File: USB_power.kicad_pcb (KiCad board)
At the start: 2 copper layers, 13 parts, among them J1 PWR_IN, J2 USB_A

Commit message: 配線完了
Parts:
- removed C3, C4: 1uF, Capacitor_SMD:C_0805_2012Metric
- added C10: 10uF, Capacitor_SMD:C_0805_2012Metric, F.Cu at (61.2, 73.7)
- added J4: USB_C_Receptacle_USB2.0_16P, Connector_USB:USB_C_Receptacle_GCT_USB4105-xx-A_16P_TopMnt_Horizontal, F.Cu at (79.0, 99.1)
- added MD2: OKL-T_6-W12N-C, USB_power:MURATA_OKL-T-6-W12N-C_0, F.Cu at (53.3, 80.0)
- added R10: 200R, Resistor_SMD:R_0805_2012Metric, F.Cu at (63.3, 79.3)
- added R6: 1k, Resistor_SMD:R_0805_2012Metric, F.Cu at (61.5, 86.3)
- added R7: 330R, Resistor_SMD:R_0805_2012Metric, F.Cu at (63.5, 84.4)
- added R8: 10R, Resistor_SMD:R_0805_2012Metric, F.Cu at (65.5, 82.7)
- added R9: 1k, Resistor_SMD:R_0805_2012Metric, F.Cu at (61.3, 77.5)
- C1, C2: value 10uF -> 22uF
- J2: value USB_A -> USB_A_Stacked; footprint Connector_USB:USB_A_CONNFLY_DS1095-WNR0 -> Connector_USB:USB_A_CUI_UJ2-ADH-TH_Horizontal_Stacked
- MD1: footprint Pi_Header:MURATA_OKL-T-6-W12N-C_0 -> USB_power:MURATA_OKL-T-6-W12N-C_0
- moved C1 34.3 mm to (52.3, 91.4)
- moved R5 33.3 mm to (63.5, 99.0), turned to -90 degrees
- moved R4 30.9 mm to (61.4, 97.0), turned to -90 degrees
- moved MD1 30.9 mm to (53.6, 99.6)
- moved R1 30.9 mm to (61.7, 105.8)
- moved R2 30.8 mm to (63.8, 104.0)
- moved R3 30.7 mm to (65.8, 102.2)
- moved C5 28.7 mm to (61.5, 93.5), turned to -90 degrees
- moved C2 22.1 mm to (52.3, 71.9)
- moved J1 18.7 mm to (51.0, 62.2), turned to 0 degrees
- moved J2 16.9 mm to (69.8, 75.4), turned to 180 degrees
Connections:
- J2 pad 1: +5V -> +5VP
- J2 pad 5: GND -> +5VP
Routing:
- net GND: track 0.00 -> 60.3 mm, vias 30 -> 11
- net +5V: track 0.00 -> 33.7 mm, vias 4 -> 0
- net +5VP: track 0.00 -> 12.5 mm
- net Net-(MD2-TRIM): track 0.00 -> 4.63 mm
- net Net-(R4-Pad2): track 0.00 -> 2.12 mm
- net Net-(R7-Pad2): track 0.00 -> 2.05 mm
- net Net-(R10-Pad1): track 0.00 -> 2.03 mm
- net Net-(R6-Pad2): track 0.00 -> 2.03 mm
- net Net-(MD1-TRIM): track 5.52 -> 4.63 mm
- added copper zone on B.Cu, net +5VP
- added copper zone on F.Cu, net +5VP
- removed copper zone on B.Cu, net +5V
- removed copper zone on F.Cu, net +5V

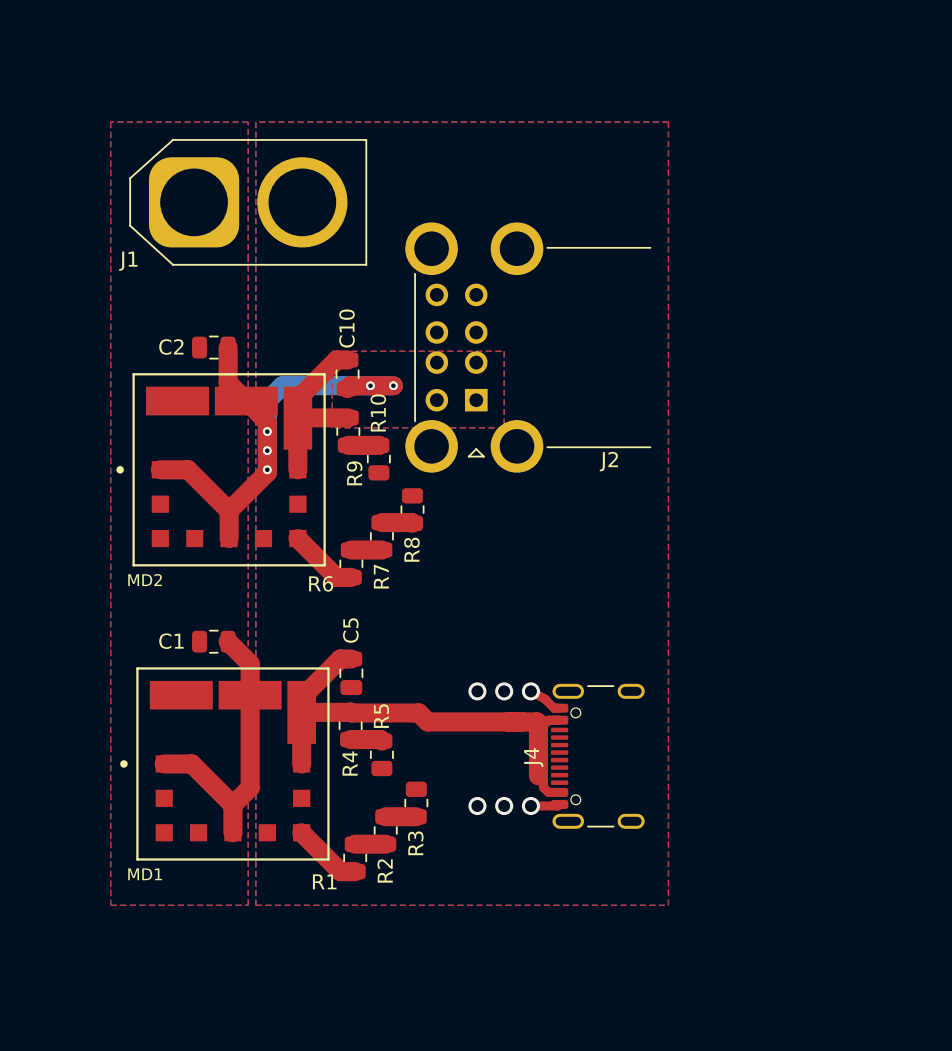
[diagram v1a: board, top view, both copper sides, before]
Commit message: XT60の向きなおした
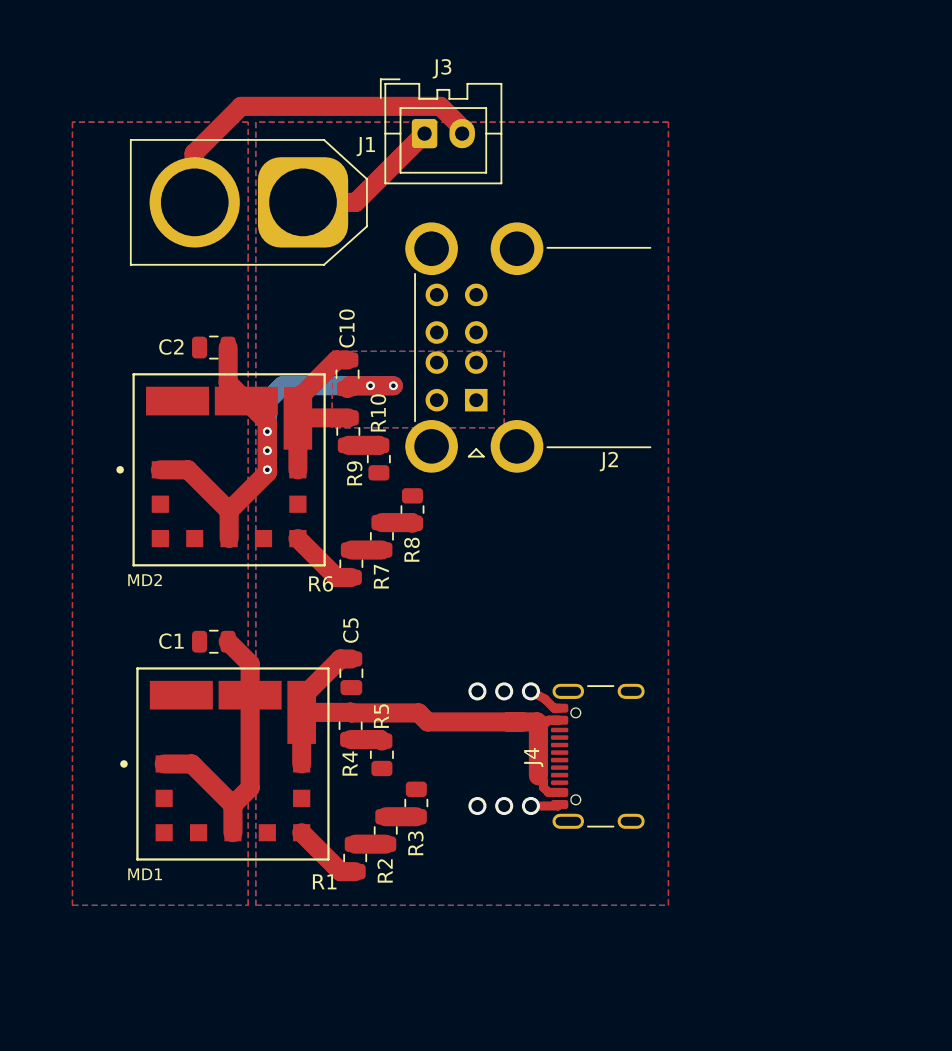
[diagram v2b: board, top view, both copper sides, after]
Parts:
- added J3: Power_check, Connector_JST:JST_XA_B02B-XASK-1_1x02_P2.50mm_Vertical, F.Cu at (66.3, 57.7)
- moved J1 7.24 mm to (58.3, 62.2), turned to 180 degrees
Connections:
- J1 pad 1: +BATT -> GND
- J1 pad 2: GND -> +BATT
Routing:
- net +BATT: track 0.00 -> 23.3 mm
- net GND: track 60.3 -> 70.3 mm

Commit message: 穴あけなど
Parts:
- removed J2: USB_A_Stacked, Connector_USB:USB_A_CUI_UJ2-ADH-TH_Horizontal_Stacked
- added H1: MountingHole, MountingHole:MountingHole_3.2mm_M3, F.Cu at (43.7, 54.4)
- added H2: MountingHole, MountingHole:MountingHole_3.2mm_M3, F.Cu at (79.2, 54.4)
- added H3: MountingHole, MountingHole:MountingHole_3.2mm_M3, F.Cu at (79.2, 112.8)
- added H4: MountingHole, MountingHole:MountingHole_3.2mm_M3, F.Cu at (43.7, 112.8)
- added J5: USB_A, Connector_USB:USB_A_CONNFLY_DS1095-WNR0, F.Cu at (68.7, 74.1)
- added J6: USB_A, Connector_USB:USB_A_CONNFLY_DS1095-WNR0, F.Cu at (68.7, 91.9)
- moved C5 4.80 mm to (57.1, 91.4), turned to 180 degrees
- moved C10 4.61 mm to (57.0, 71.9), turned to 180 degrees
- moved J4 3.56 mm to (79.0, 102.6)
- moved R5 1.37 mm to (63.5, 100.3)
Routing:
- net +5V: track 33.7 -> 12.4 mm, vias 0 -> 5
- net GND: track 70.3 -> 52.4 mm, vias 11 -> 30
- net Net-(R4-Pad2): track 2.12 -> 3.10 mm
- net +5VP: track 12.5 -> 11.5 mm, vias 0 -> 12
- net +BATT: track 23.3 -> 23.5 mm, vias 0 -> 44
- added copper zone on B.Cu, net +5V
- added copper zone on F.Cu, net +5V
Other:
- board outline added: 42.5 x 65.5 mm
- board text added: "12V IN"
- board text added: "5V OUT"
- board text added: "JLCJLCJLCJLC"

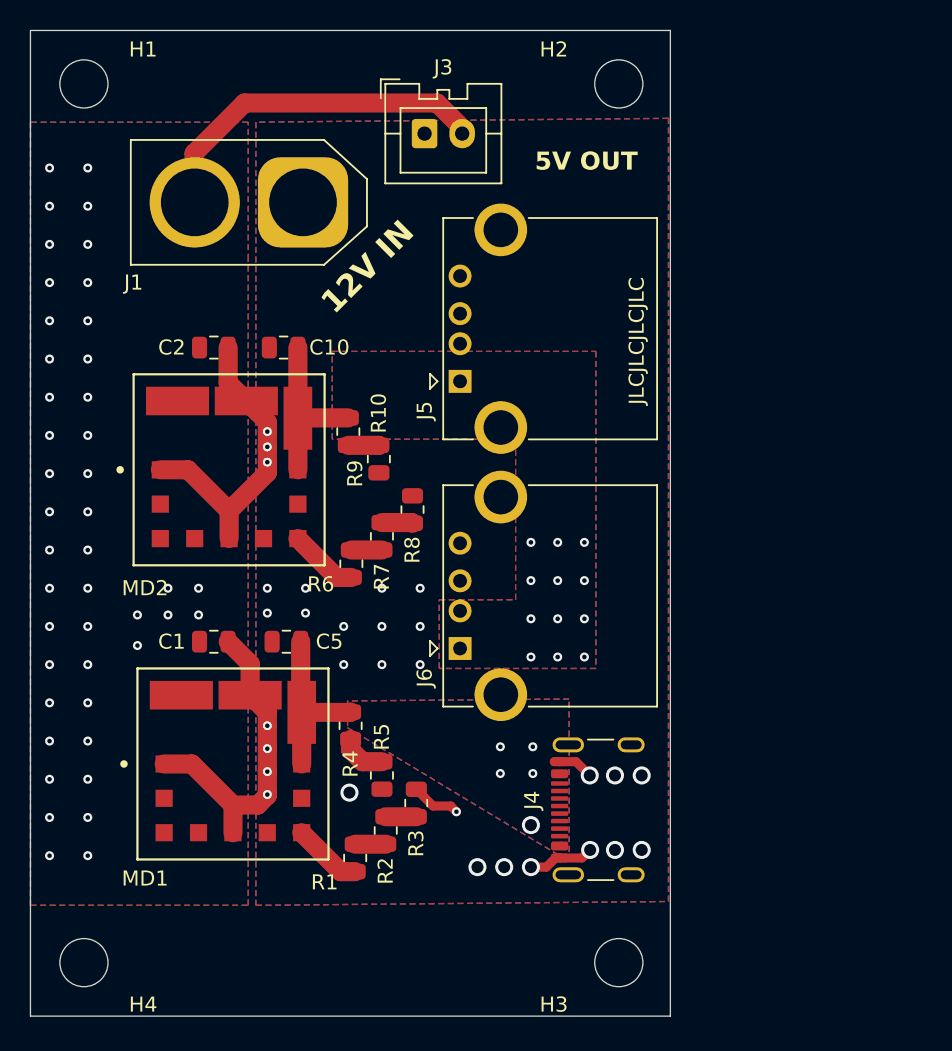
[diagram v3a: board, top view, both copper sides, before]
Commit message: PCB: 5V確認用LED配置
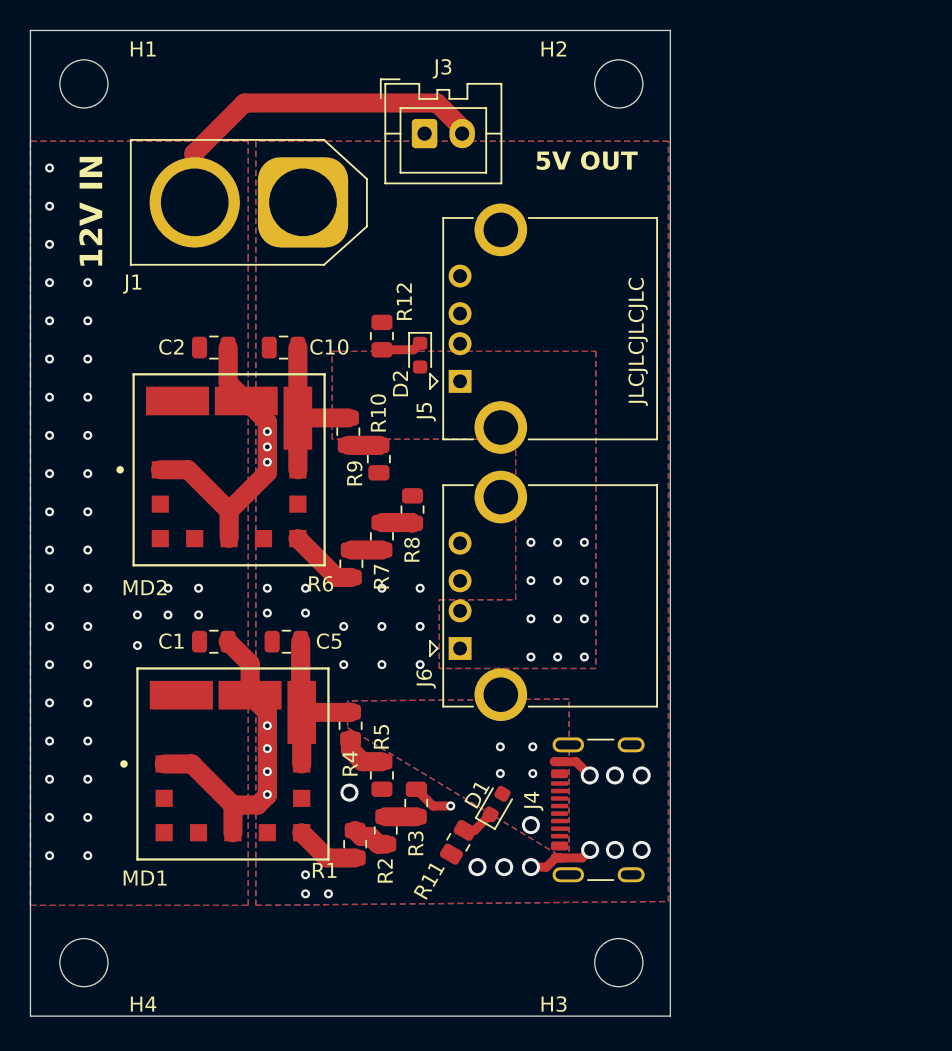
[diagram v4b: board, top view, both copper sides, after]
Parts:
- added D1: LED, LED_SMD:LED_0603_1608Metric, F.Cu at (71.1, 102.2)
- added D2: LED, LED_SMD:LED_0603_1608Metric, F.Cu at (66.0, 72.4)
- added R11: 10k, Resistor_SMD:R_0805_2012Metric, F.Cu at (68.6, 104.8)
- added R12: 10k, Resistor_SMD:R_0805_2012Metric, F.Cu at (63.5, 71.1)
- moved R1 0.91 mm to (61.7, 104.9)
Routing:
- net Net-(D2-K): track 0.00 -> 2.72 mm
- net Net-(D1-K): track 0.00 -> 2.13 mm
- net GND: track 52.4 -> 51.8 mm, vias 30 -> 33
- net +BATT: vias 44 -> 41

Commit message: USBコネクタ構成変更: stucked_A、A、C
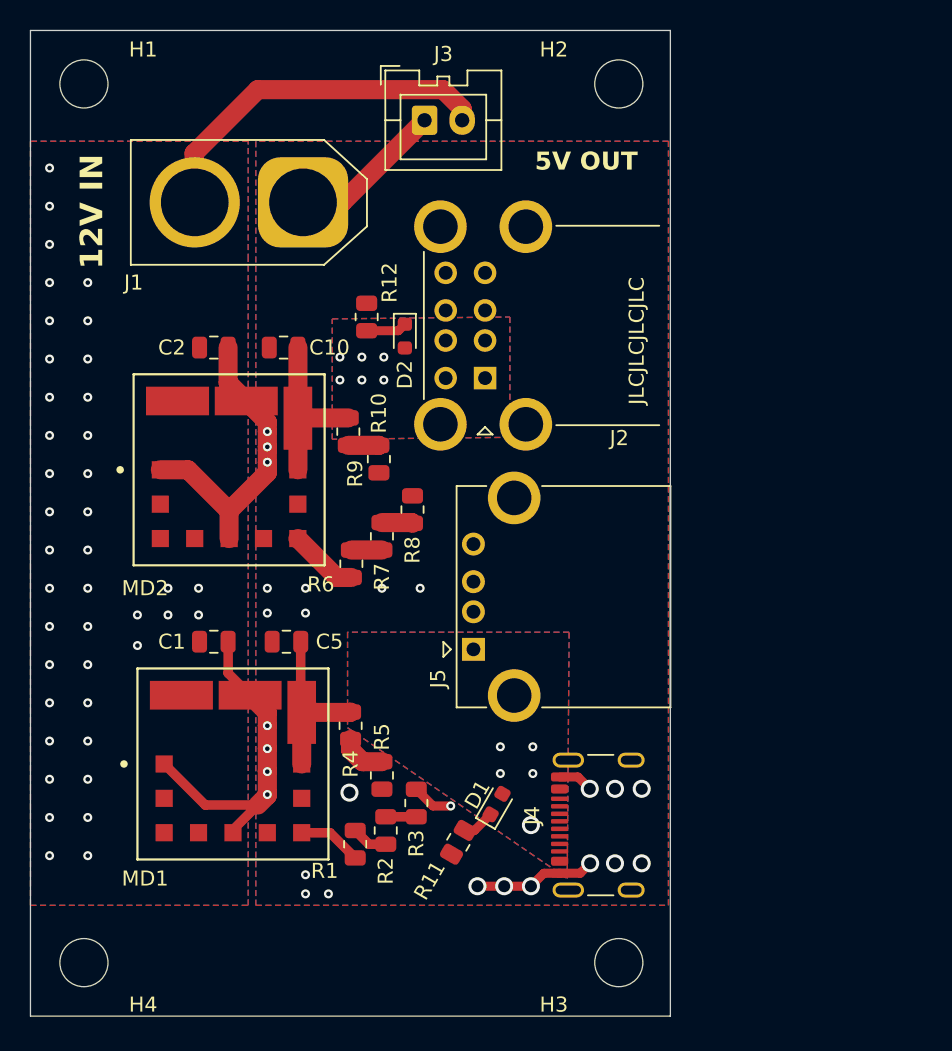
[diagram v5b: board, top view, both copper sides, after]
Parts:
- removed J6: USB_A, Connector_USB:USB_A_CONNFLY_DS1095-WNR0
- added J2: USB_A_Stacked, Connector_USB:USB_A_CUI_UJ2-ADH-TH_Horizontal_Stacked, F.Cu at (70.4, 73.9)
- moved J5 17.8 mm to (69.6, 91.9)
- moved R12 1.63 mm to (62.5, 69.8)
- moved D2 1.63 mm to (65.0, 71.1)
- moved J4 1.02 mm to (79.0, 103.6)
- moved J3 0.89 mm to (66.3, 56.8)
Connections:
- J5 pad 1: +5VP -> +5V
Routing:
- net GND: track 51.8 -> 66.3 mm, vias 33 -> 27
- net +BATT: track 23.5 -> 24.1 mm
- net +5VP: vias 12 -> 6
